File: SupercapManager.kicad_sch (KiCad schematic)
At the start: 7 parts, among them J1 JST4_M, J2 XT30_M, J3 XT30_M, J4 XT30_M, J5 XT30_M, Q11 BSC059N04LS6, Q12 BSC059N04LS6

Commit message: Considering using a different IC for 1st stage
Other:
- sheet Output Boost (Stage 2) ports: added +5.5V_{IN}; removed +6V_{IN}
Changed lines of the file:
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@@
 			)
 		)
-		(pin "+6V_{IN}" input
+		(pin "+5.5V_{IN}" input
 			(at 171.45 119.38 180)
 			(effects

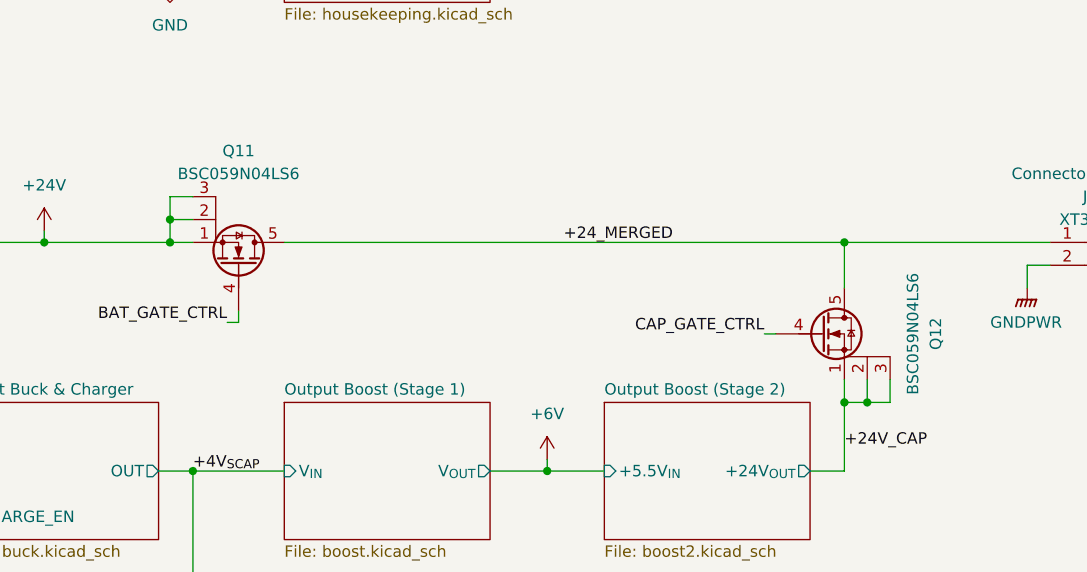
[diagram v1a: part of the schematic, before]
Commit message: Redesigning output boosts to be more efficient albeit with less current capacity
idk what I changed with the schematics lol
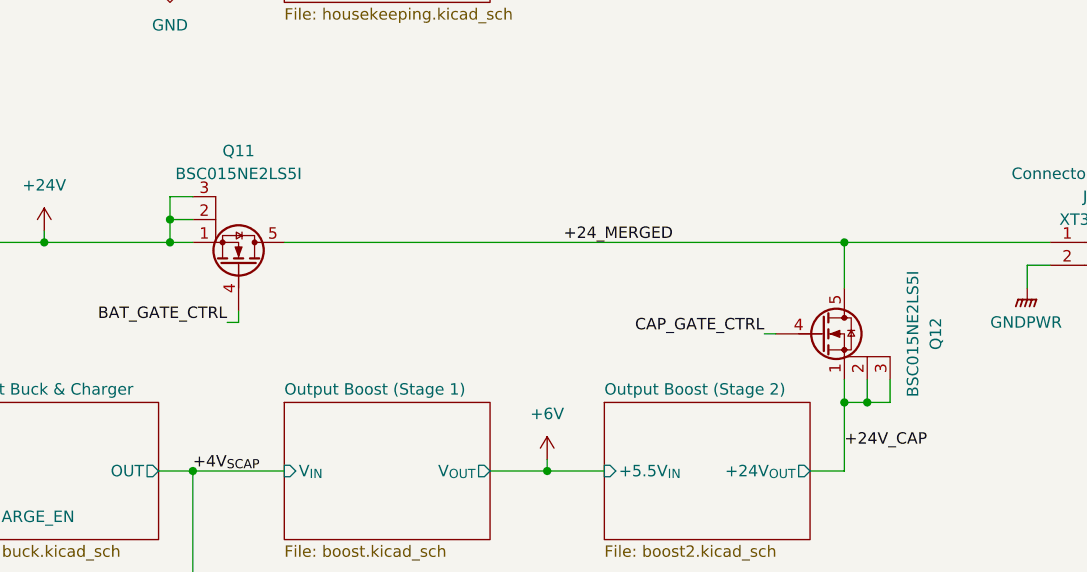
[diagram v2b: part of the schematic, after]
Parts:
- Q11, Q12: value BSC059N04LS6 -> BSC015NE2LS5I; Mouser Part Number 726-BSC059N04LS6ATMA -> 726-BSC015NE2LS5IATM
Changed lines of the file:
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@@
 			)
 		)
-		(property "Value" "BSC059N04LS6"
+		(property "Value" "BSC015NE2LS5I"
 			(at 130.81 86.36 90)
 			(effects
@@
 			)
 		)
-		(property "Datasheet" "https://www.mouser.com/datasheet/2/196/Infineon_BSC059N04LS6_DataSheet_v02_01_EN-3360636.pdf"
+		(property "Datasheet" "https://www.mouser.com/datasheet/2/196/Infineon_BSC015NE2LS5I_DataSheet_v02_01_EN-3360635.pdf"
 			(at 130.81 96.52 0)
 			(effects
@@
 			)
 		)
-		(property "Mouser Part Number" "726-BSC059N04LS6ATMA"
+		(property "Mouser Part Number" "726-BSC015NE2LS5IATM"
 			(at 130.81 96.52 0)
 			(effects
@@
 			)
 		)
-		(property "Value" "BSC059N04LS6"
+		(property "Value" "BSC015NE2LS5I"
 			(at 205.74 104.14 90)
 			(effects
@@
 			)
 		)
-		(property "Datasheet" "https://www.mouser.com/datasheet/2/196/Infineon_BSC059N04LS6_DataSheet_v02_01_EN-3360636.pdf"
+		(property "Datasheet" "https://www.mouser.com/datasheet/2/196/Infineon_BSC015NE2LS5I_DataSheet_v02_01_EN-3360635.pdf"
 			(at 195.58 104.14 0)
 			(effects
@@
 			)
 		)
-		(property "Mouser Part Number" "726-BSC059N04LS6ATMA"
+		(property "Mouser Part Number" "726-BSC015NE2LS5IATM"
 			(at 195.58 104.14 0)
 			(effects

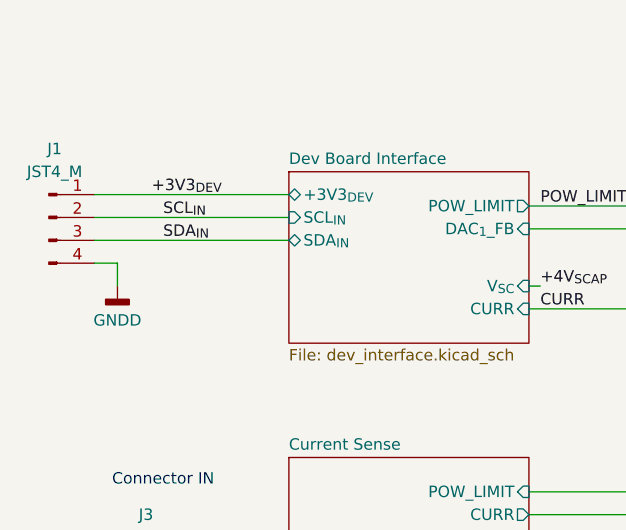
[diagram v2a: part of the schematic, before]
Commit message: Find suitable op-amp for buffer in current sense
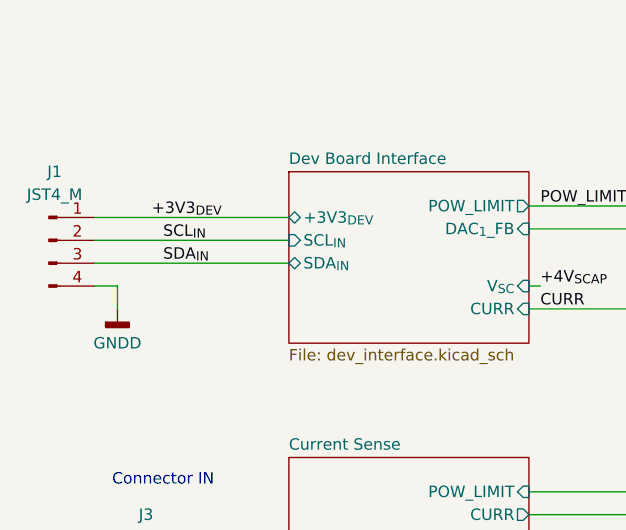
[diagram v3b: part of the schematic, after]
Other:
- moved on the sheet: J1
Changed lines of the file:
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@@
 	(wire
 		(pts
-			(xy 29.21 63.5) (xy 29.21 60.96)
+			(xy 29.21 66.04) (xy 29.21 63.5)
 		)
 		(stroke
@@
 	(wire
 		(pts
+			(xy 26.67 58.42) (xy 48.26 58.42)
+		)
+		(stroke
+			(width 0)
+			(type default)
+		)
+	)
+	(wire
+		(pts
+			(xy 198.12 109.22) (xy 198.12 111.76)
+		)
+		(stroke
+			(width 0)
+			(type default)
+		)
+	)
+	(wire
+		(pts
+			(xy 125.73 119.38) (xy 135.89 119.38)
+		)
+		(stroke
+			(width 0)
+			(type default)
+		)
+	)
+	(wire
+		(pts
+			(xy 158.75 119.38) (xy 165.1 119.38)
+		)
+		(stroke
+			(width 0)
+			(type default)
+		)
+	)
+	(wire
+		(pts
+			(xy 88.9 57.15) (xy 88.9 86.36)
+		)
+		(stroke
+			(width 0)
+			(type default)
+		)
+	)
+	(wire
+		(pts
+			(xy 218.44 99.06) (xy 218.44 96.52)
+		)
+		(stroke
+			(width 0)
+			(type default)
+		)
+	)
+	(wire
+		(pts
+			(xy 123.19 62.23) (xy 120.65 62.23)
+		)
+		(stroke
+			(width 0)
+			(type default)
+		)
+	)
+	(wire
+		(pts
+			(xy 26.67 60.96) (xy 48.26 60.96)
+		)
+		(stroke
+			(width 0)
+			(type default)
+		)
+	)
+	(wire
+		(pts
+			(xy 194.31 119.38) (xy 198.12 119.38)
+		)
+		(stroke
+			(width 0)
+			(type default)
+		)
+	)
+	(wire
+		(pts
 			(xy 26.67 55.88) (xy 48.26 55.88)
 		)
@@
 	(wire
 		(pts
-			(xy 198.12 109.22) (xy 198.12 111.76)
-		)
-		(stroke
-			(width 0)
-			(type default)
-		)
-	)
-	(wire
-		(pts
-			(xy 125.73 119.38) (xy 135.89 119.38)
-		)
-		(stroke
-			(width 0)
-			(type default)
-		)
-	)
-	(wire
-		(pts
-			(xy 158.75 119.38) (xy 165.1 119.38)
-		)
-		(stroke
-			(width 0)
-			(type default)
-		)
-	)
-	(wire
-		(pts
-			(xy 88.9 57.15) (xy 88.9 86.36)
-		)
-		(stroke
-			(width 0)
-			(type default)
-		)
-	)
-	(wire
-		(pts
-			(xy 218.44 99.06) (xy 218.44 96.52)
-		)
-		(stroke
-			(width 0)
-			(type default)
-		)
-	)
-	(wire
-		(pts
-			(xy 123.19 62.23) (xy 120.65 62.23)
-		)
-		(stroke
-			(width 0)
-			(type default)
-		)
-	)
-	(wire
-		(pts
-			(xy 26.67 58.42) (xy 48.26 58.42)
-		)
-		(stroke
-			(width 0)
-			(type default)
-		)
-	)
-	(wire
-		(pts
-			(xy 194.31 119.38) (xy 198.12 119.38)
-		)
-		(stroke
-			(width 0)
-			(type default)
-		)
-	)
-	(wire
-		(pts
-			(xy 26.67 53.34) (xy 48.26 53.34)
-		)
-		(stroke
-			(width 0)
-			(type default)
-		)
-	)
-	(wire
-		(pts
 			(xy 200.66 111.76) (xy 203.2 111.76)
 		)
@@
 	(wire
 		(pts
-			(xy 29.21 60.96) (xy 26.67 60.96)
+			(xy 29.21 63.5) (xy 26.67 63.5)
 		)
 		(stroke
@@
 	)
 	(label "SDA_{IN}"
-		(at 34.29 58.42 0)
+		(at 34.29 60.96 0)
 		(effects
 			(font
@@
 	)
 	(label "SCL_{IN}"
-		(at 34.29 55.88 0)
+		(at 34.29 58.42 0)
 		(effects
 			(font
@@
 	)
 	(label "+3V3_{DEV}"
-		(at 33.02 53.34 0)
+		(at 33.02 55.88 0)
 		(effects
 			(font
@@
 	(symbol
 		(lib_id "power:GNDD")
-		(at 29.21 63.5 0)
+		(at 29.21 66.04 0)
 		(unit 1)
 		(exclude_from_sim no)
@@
 		(fields_autoplaced yes)
 		(property "Reference" "#PWR03"
+			(at 29.21 72.39 0)
+			(effects
+				(font
+					(size 1.27 1.27)
+				)
+				(hide yes)
+			)
+		)
+		(property "Value" "GNDD"
 			(at 29.21 69.85 0)
 			(effects
@@
 					(size 1.27 1.27)
 				)
-				(hide yes)
-			)
-		)
-		(property "Value" "GNDD"
-			(at 29.21 67.31 0)
-			(effects
-				(font
-					(size 1.27 1.27)
-				)
 			)
 		)
 		(property "Footprint" ""
-			(at 29.21 63.5 0)
+			(at 29.21 66.04 0)
 			(effects
 				(font
@@
 		)
 		(property "Datasheet" ""
-			(at 29.21 63.5 0)
+			(at 29.21 66.04 0)
 			(effects
 				(font
@@
 		)
 		(property "Description" "Power symbol creates a global label with name \"GNDD\" , digital ground"
-			(at 29.21 63.5 0)
+			(at 29.21 66.04 0)
 			(effects
 				(font
@@
 	(symbol
 		(lib_id "Connector:Conn_01x04_Pin")
-		(at 21.59 55.88 0)
+		(at 21.59 58.42 0)
 		(unit 1)
 		(exclude_from_sim no)
@@
 		(fields_autoplaced yes)
 		(property "Reference" "J1"
-			(at 22.225 48.26 0)
+			(at 22.225 50.8 0)
 			(effects
 				(font
@@
 		)
 		(property "Value" "JST4_M"
-			(at 22.225 50.8 0)
+			(at 22.225 53.34 0)
 			(effects
 				(font
@@
 		)
 		(property "Footprint" "Connector_JST:JST_GH_BM04B-GHS-TBT_1x04-1MP_P1.25mm_Vertical"
-			(at 21.59 55.88 0)
+			(at 21.59 58.42 0)
 			(effects
 				(font
@@
 		)
 		(property "Datasheet" "~"
-			(at 21.59 55.88 0)
+			(at 21.59 58.42 0)
 			(effects
 				(font
@@
 		)
 		(property "Description" "Generic connector, single row, 01x04, script generated"
-			(at 21.59 55.88 0)
+			(at 21.59 58.42 0)
 			(effects
 				(font
@@
 		)
 		(property "Sim.Device" ""
-			(at 21.59 55.88 0)
+			(at 21.59 58.42 0)
 			(effects
 				(font
@@
 		)
 		(property "Sim.Pins" ""
-			(at 21.59 55.88 0)
+			(at 21.59 58.42 0)
 			(effects
 				(font
@@
 		)
 		(property "Sim.Type" ""
-			(at 21.59 55.88 0)
+			(at 21.59 58.42 0)
 			(effects
 				(font
@@
 		)
 		(property "Height" ""
-			(at 21.59 55.88 0)
+			(at 21.59 58.42 0)
 			(effects
 				(font
@@
 		)
 		(property "Manufacturer_Name" ""
-			(at 21.59 55.88 0)
+			(at 21.59 58.42 0)
 			(effects
 				(font
@@
 		)
 		(property "Manufacturer_Part_Number" ""
-			(at 21.59 55.88 0)
+			(at 21.59 58.42 0)
 			(effects
 				(font
@@
 		)
 		(property "Mouser Price/Stock" ""
-			(at 21.59 55.88 0)
+			(at 21.59 58.42 0)
 			(effects
 				(font
@@
 		)
 		(pin "SCL_{IN}" input
+			(at 48.26 58.42 180)
+			(effects
+				(font
+					(size 1.27 1.27)
+				)
+				(justify left)
+			)
+		)
+		(pin "+3V3_{DEV}" bidirectional
 			(at 48.26 55.88 180)
 			(effects
@@
 			)
 		)
-		(pin "+3V3_{DEV}" bidirectional
-			(at 48.26 53.34 180)
-			(effects
-				(font
-					(size 1.27 1.27)
-				)
-				(justify left)
-			)
-		)
 		(pin "SDA_{IN}" bidirectional
-			(at 48.26 58.42 180)
-			(effects
-				(font
+			(at 48.26 60.96 180)
+			(effects
+				(font
